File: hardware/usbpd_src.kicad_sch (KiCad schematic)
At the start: 37 parts, among them J201 USB_C_Receptacle_USB2.0, Q601 DMP3028, Q602 DMP3028, Q603 DMP3028, Q604 MMBT3904, Q605 MMBT3904, Q606 DMP3028, Q607 MMBT3904, U201 SRV05-4, U602 INA381A2IDSGR, U603 BL1551B

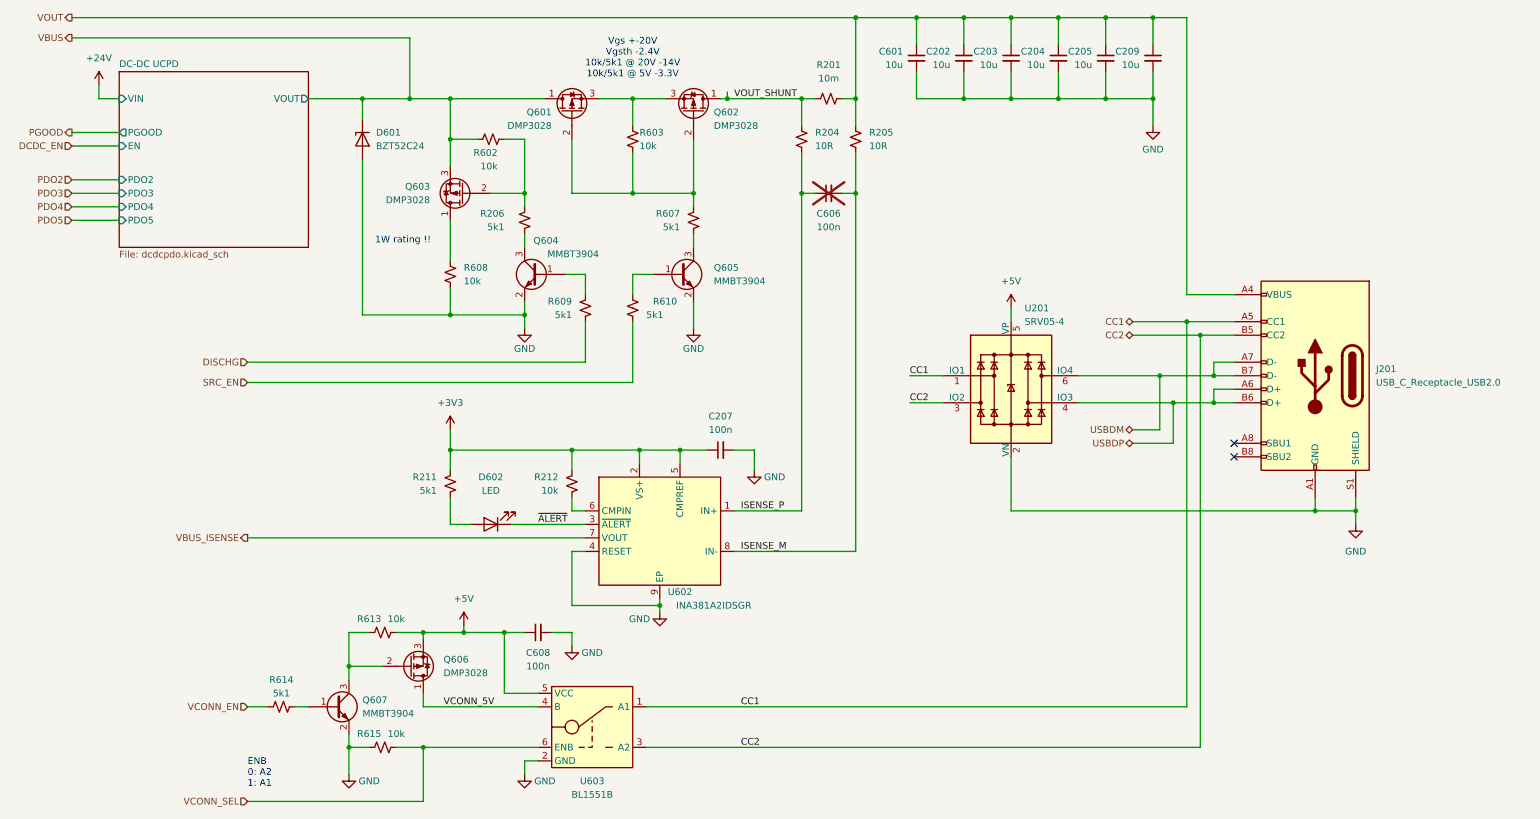
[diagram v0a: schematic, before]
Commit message: Fix SiC437 footprint and LCSC field error
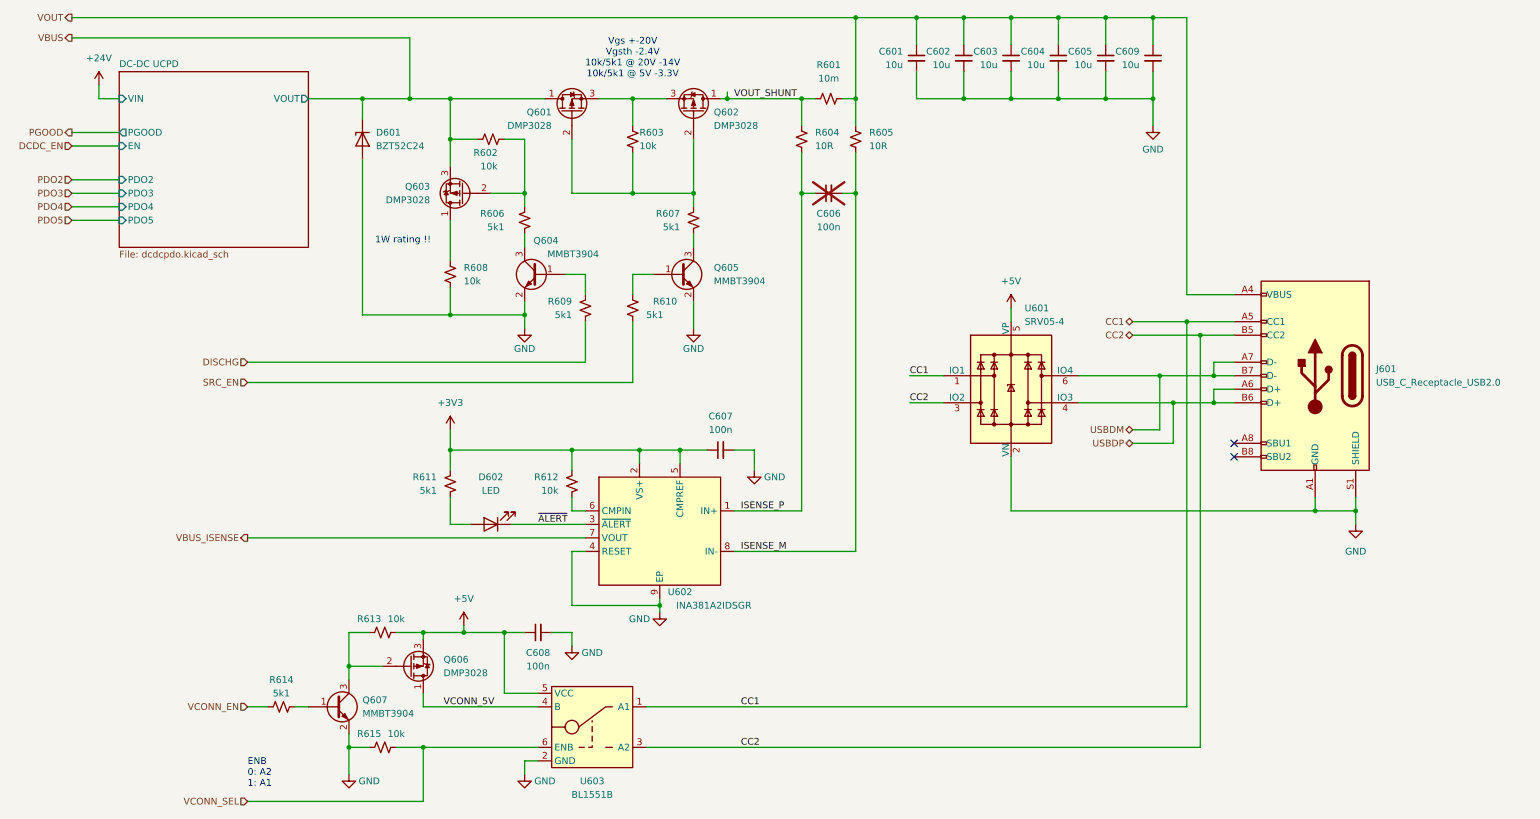
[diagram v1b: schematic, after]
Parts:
- C601: LCSC ID (none) -> C96446; LCSC Part C96446 -> (none)
- C602: renamed from C202; LCSC ID (none) -> C96446; LCSC Part C96446 -> (none)
- C603: renamed from C203; LCSC ID (none) -> C96446; LCSC Part C96446 -> (none)
- C604: renamed from C204; LCSC ID (none) -> C96446; LCSC Part C96446 -> (none)
- C605: renamed from C205; LCSC ID (none) -> C96446; LCSC Part C96446 -> (none)
- C606: LCSC ID (none) -> C14663; LCSC Part C14663 -> (none)
- C607: renamed from C207; LCSC ID (none) -> C307331; LCSC Part C307331 -> (none)
- C608: LCSC ID (none) -> C307331; LCSC Part C307331 -> (none)
- C609: renamed from C209; LCSC ID (none) -> C96446; LCSC Part C96446 -> (none)
- D601: LCSC ID (none) -> C727011; LCSC Part C727011 -> (none)
- D602: LCSC ID (none) -> C2290; LCSC Part C2290 -> (none)
- J601: renamed from J201; LCSC ID (none) -> C165948; LCSC Part C165948 -> (none)
- Q601, Q602, Q603, Q606: LCSC ID (none) -> C150441; LCSC Part C150441 -> (none)
- Q604, Q605, Q607: LCSC ID (none) -> C20526; LCSC Part C20526 -> (none)
- R601: renamed from R201; LCSC ID (none) -> C2961483; LCSC Part C2961483 -> (none)
- R602, R603, R613, R615: LCSC ID (none) -> C25744; LCSC Part C25744 -> (none)
- R604: renamed from R204; LCSC ID (none) -> C25077; LCSC Part C25077 -> (none)
- R605: renamed from R205; LCSC ID (none) -> C25077; LCSC Part C25077 -> (none)
- R606: renamed from R206; LCSC ID (none) -> C25905; LCSC Part C25905 -> (none)
- R607, R609, R610, R614: LCSC ID (none) -> C25905; LCSC Part C25905 -> (none)
- R608: LCSC ID (none) -> C25804; LCSC Part C25804 -> (none)
- R611: renamed from R211; LCSC ID (none) -> C25905; LCSC Part C25905 -> (none)
- R612: renamed from R212; LCSC ID (none) -> C25744; LCSC Part C25744 -> (none)
- U601: renamed from U201; LCSC ID (none) -> C7420376; LCSC Part C7420376 -> (none)
- U602: LCSC ID (none) -> C2155688; LCSC Part C2155688 -> (none)
- U603: LCSC ID (none) -> C2944066; LCSC Part C2944066 -> (none)
